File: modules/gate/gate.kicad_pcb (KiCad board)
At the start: 2 copper layers, 30.5 x 68.6 mm, 24 parts, among them SW1 MODE SELECT, U1 MCP6002-xSN, U2 ATtiny1616-M, U3 MCP6002-xSN

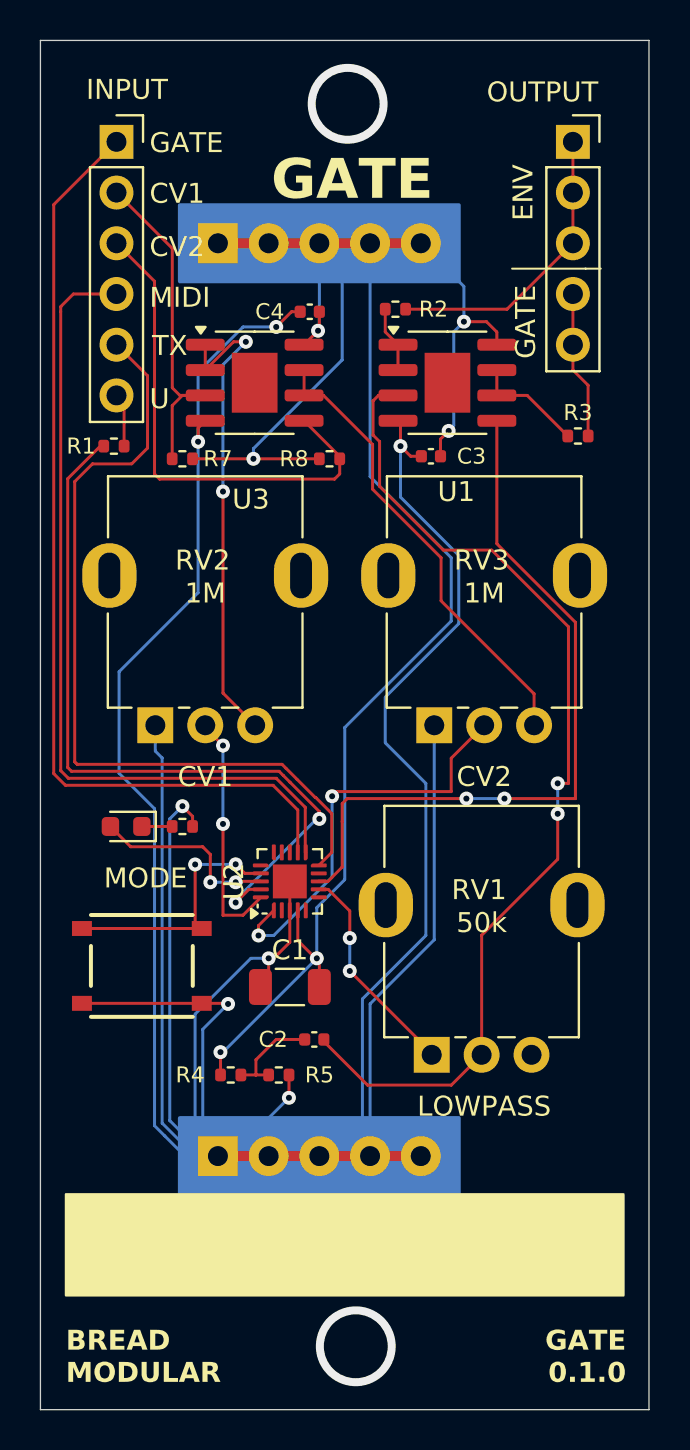
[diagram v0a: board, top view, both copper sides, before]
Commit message: Apply new code changes to the schematic
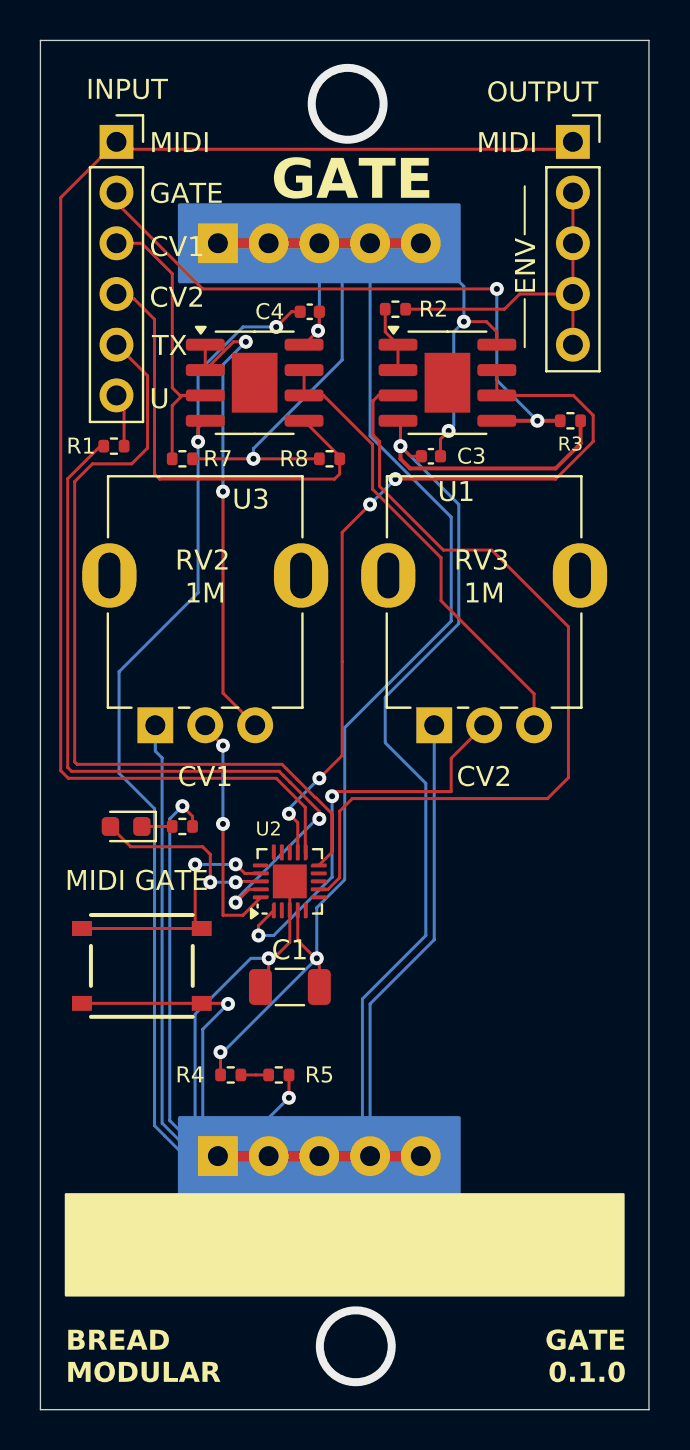
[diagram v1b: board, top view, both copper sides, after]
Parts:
- removed C2: 100nf, Capacitor_SMD:C_0402_1005Metric
- removed RV1: 50k, BreadModular_Pots:Potentiometer_RV09
- D1: value LED -> GATE MODE LED
- R3: value 1k -> 100k
- SW1: value MODE SELECT -> GATE MODE SELECT
- moved R3 0.85 mm to (73.5, 59.7), turned to 180 degrees
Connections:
- INPUT1 pad 1: GATE -> MIDI
- INPUT1 pad 2: CV1 -> GATE
- INPUT1 pad 3: CV2 -> CV1
- INPUT1 pad 4: MIDI -> CV2
- OUTPUT1 pad 1: ENV_OUT -> MIDI
- OUTPUT1 pad 4: GATE_OUT -> ENV_OUT
- OUTPUT1 pad 5: GATE_OUT -> ENV_OUT
- R3 pad 1: Net-(U1B--) -> GND
- R3 pad 2: GATE_OUT -> GATE
- U1 pad 5: Net-(U1B-+) -> GATE
- U1 pad 6: Net-(U1B--) -> BUFF_GATE
- U1 pad 7: Net-(U1B--) -> BUFF_GATE
- U2 pad 12: GATE -> BUFF_GATE
- U2 pad 7: Net-(U2-PA6) -> Net-(U1A-+)
- U2 pad 8: Net-(U1B-+) -> unconnected-(U2-PA7-Pad8)
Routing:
- net BUFF_GATE: track 0.00 -> 39.6 mm, vias 0 -> 4
- net Net-(U1B-+): track 37.0 -> 0.00 mm, vias 2 -> 0
- net MIDI: track 41.6 -> 71.7 mm
- net GATE: track 48.0 -> 32.0 mm, vias 0 -> 2
- net GND: track 209.5 -> 221.0 mm
- net Net-(U2-PA6): track 10.9 -> 0.00 mm, vias 2 -> 0
- net Net-(U1A-+): track 51.2 -> 42.5 mm, vias 2 -> 0
- net GATE_OUT: track 7.43 -> 0.00 mm
- net Net-(U1B--): track 5.66 -> 0.00 mm
- net V_MID: track 5.01 -> 1.39 mm
- net CV2: track 25.2 -> 22.7 mm
- net CV1: track 17.3 -> 15.5 mm
- net ENV_OUT: track 14.8 -> 16.3 mm
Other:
- board text added: "MIDI GATE"
- board text removed: "LOWPASS"
- board text removed: "MODE"

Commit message: Add algo mode select to pcb
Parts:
- added D2: ALGO MODE LED, LED_SMD:LED_0603_1608Metric, F.Cu at (72.8, 80.0)
- added R9: 330, Resistor_SMD:R_0402_1005Metric, F.Cu at (69.7, 80.0)
- added SW2: ALGO MODE SELECT, BreadModular_MISC:SPST_TS-1187A-B-A-B, F.Cu at (71.6, 87.0)
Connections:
- U2 pad 15: unconnected-(U2-PC0-Pad15) -> Net-(SW2-B)
- U2 pad 16: unconnected-(U2-PC1-Pad16) -> Net-(D2-A)
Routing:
- net GND: track 221.0 -> 261.1 mm, vias 7 -> 9
- net Net-(SW2-B): track 0.00 -> 30.4 mm, vias 0 -> 2
- net Net-(D2-A): track 0.00 -> 24.3 mm, vias 0 -> 2
- net Net-(D2-K): track 0.00 -> 1.88 mm
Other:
- board text added: "ALGO SELECT"

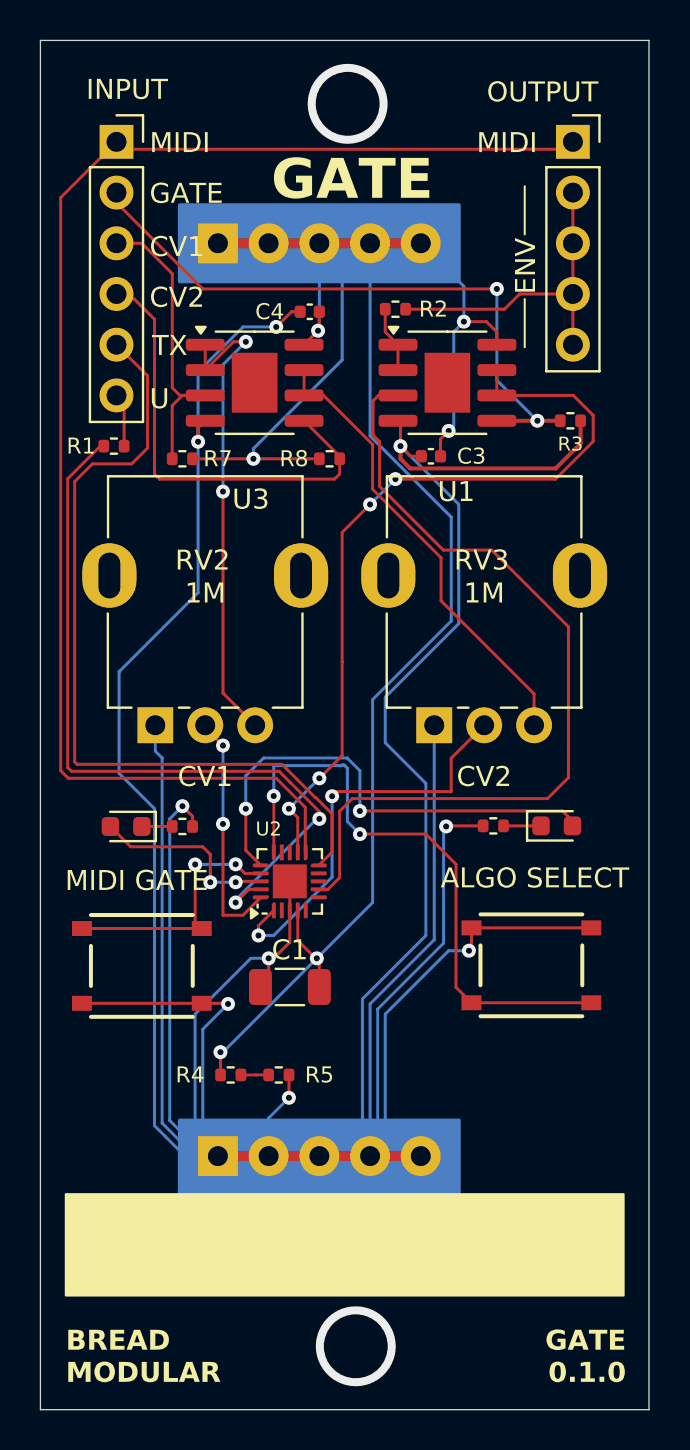
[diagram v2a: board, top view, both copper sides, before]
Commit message: Add LED Preview
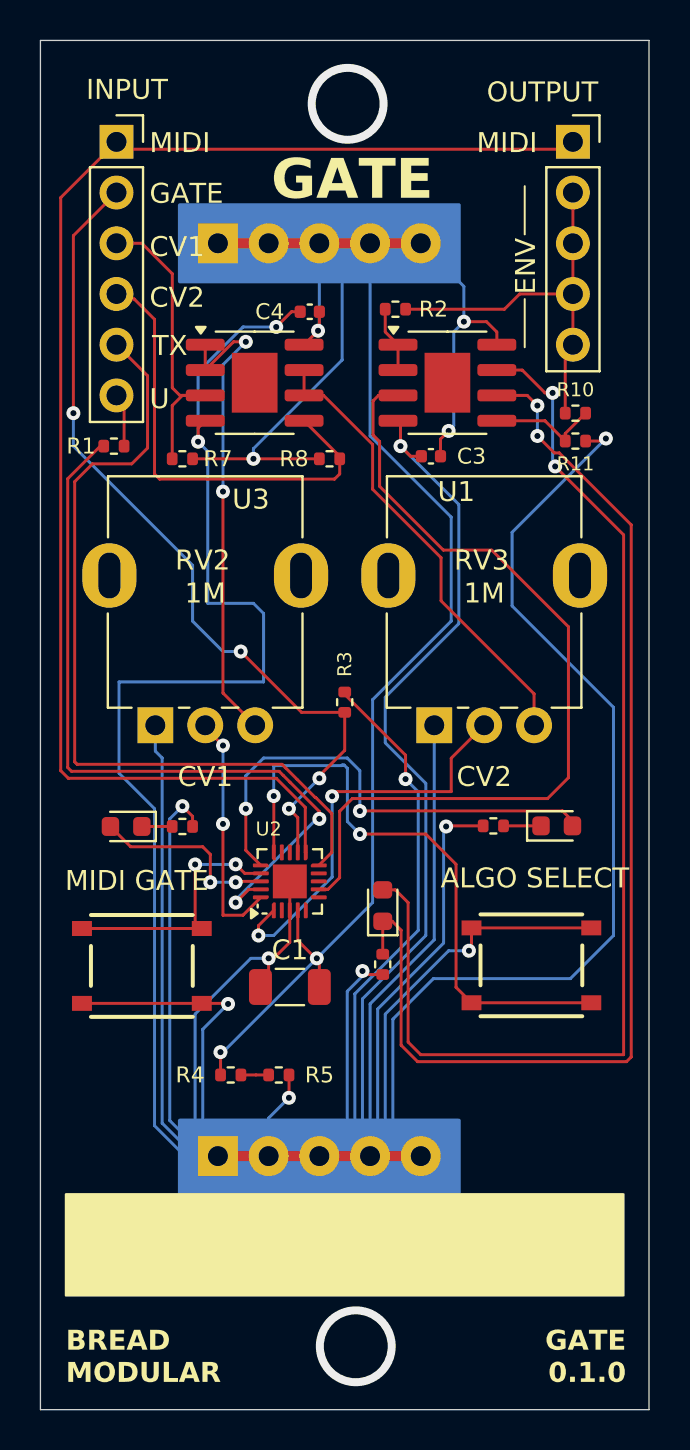
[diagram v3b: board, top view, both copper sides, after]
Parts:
- added D3: ENV LED, LED_SMD:LED_0603_1608Metric, F.Cu at (64.1, 84.0)
- added R10: 100k, Resistor_SMD:R_0402_1005Metric, F.Cu at (73.8, 59.3)
- added R11: 100k, Resistor_SMD:R_0402_1005Metric, F.Cu at (73.8, 60.7)
- added R12: 4.7k, Resistor_SMD:R_0402_1005Metric, F.Cu at (64.1, 86.9)
- moved R3 18.1 mm to (62.2, 73.8), turned to -90 degrees
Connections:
- INPUT1 pad 2: GATE -> BUFF_GATE
- R3 pad 2: GATE -> BUFF_GATE
- U1 pad 5: GATE -> Net-(U1B-+)
- U1 pad 6: BUFF_GATE -> Net-(D3-K)
- U1 pad 7: BUFF_GATE -> Net-(D3-A)
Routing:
- net GND: track 261.1 -> 342.3 mm, vias 9 -> 12
- net Net-(D3-A): track 0.00 -> 57.5 mm, vias 0 -> 2
- net Net-(D3-K): track 0.00 -> 57.4 mm, vias 0 -> 2
- net GATE: track 32.0 -> 0.00 mm, vias 2 -> 0
- net Net-(U1B-+): track 0.00 -> 5.67 mm
- net ENV_OUT: track 16.3 -> 19.9 mm
- net BUFF_GATE: track 39.6 -> 42.7 mm
